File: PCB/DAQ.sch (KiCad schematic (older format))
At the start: 6 parts, among them J1 Arduino_Mega_Header, U1 SDshield, U2 RTC, U3 ADC, U4 NOKIA5110, U5 DAC

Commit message: PCB Improvement
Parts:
- added J2, J8: Conn_01x07, Pin_Headers:Pin_Header_Straight_1x07_Pitch2.54mm, symbol Conn_01x07
- added J3, J4, J7: Conn_01x08, Pin_Headers:Pin_Header_Straight_1x08_Pitch2.54mm, symbol Conn_01x08
- added J5: Conn_02x18_Counter_Clockwise, Pin_Headers:Pin_Header_Straight_2x18_Pitch2.54mm, symbol Conn_02x18_Counter_Clockwise
- added J6: Conn_01x10, Pin_Headers:Pin_Header_Straight_1x10_Pitch2.54mm, symbol Conn_01x10
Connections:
- net 3.3V: now also J2.3 (Pin_3)
- net 5V: now also J5.2 (Pin_2)
- net GND: now also J2.5 (Pin_5), J5.36 (Pin_36), J6.4 (Pin_4)
- net PIN2: now also J7.6 (Pin_6)
- net PIN3: now also J7.5 (Pin_5)
- net PIN31: now also J5.12 (Pin_12)
- net PIN33: now also J5.14 (Pin_14)
- net PIN35: now also J5.16 (Pin_16)
- net PIN4: now also J7.4 (Pin_4)
- net PIN5: now also J7.3 (Pin_3)
- net PIN50: now also J5.30 (Pin_30)
- net PIN51: now also J5.32 (Pin_32)
- net PIN52: now also J5.34 (Pin_34)
- net PIN6: now also J7.2 (Pin_2)
- net PIN7: now also J7.1 (Pin_1)
- net SCL: now also J6.1 (Pin_1)
- net SDA: now also J6.2 (Pin_2)
- new net 5v: J2.4 (Pin_4)
- no-connect marks 73 -> 137
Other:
- moved on the sheet: U1, U2, U3, U4, U5

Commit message: PCB Improvements
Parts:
- added C1: 100uF, Capacitors_THT:C_Axial_L12.0mm_D6.5mm_P15.00mm_Horizontal, symbol C
- added C2: 0.1uF, Capacitors_THT:CP_Axial_L11.0mm_D6.0mm_P18.00mm_Horizontal, symbol C
- added C3: 10uF, Capacitors_THT:CP_Axial_L11.0mm_D6.0mm_P18.00mm_Horizontal, symbol C
- added C4: 1uF, Capacitors_THT:CP_Axial_L11.0mm_D6.0mm_P18.00mm_Horizontal, symbol C
- added CC+1, CC-1: 0.01uF, Capacitors_THT:CP_Axial_L11.0mm_D6.0mm_P18.00mm_Horizontal, symbol C
- added CF+1, CF-1: 100uF, Capacitors_THT:C_Axial_L3.8mm_D2.6mm_P7.50mm_Horizontal, symbol C
- added DX+1, DX-1: D_Schottky, Diodes_THT:D_A-405_P12.70mm_Horizontal, symbol D_Schottky
- added IC1: MAX743CWE+, Housings_DIP:DIP-16_W7.62mm, symbol MAX743CWE+
- added LX+1, LX-1: 100uH, Inductors_THT:L_Axial_L9.5mm_D4.0mm_P12.70mm_Horizontal_Fastron_SMCC, symbol L
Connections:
- net 5V: now also C1.1, C2.2, IC1.12 (V+(3)), IC1.13 (V+(4)), IC1.3 (AV+), IC1.4 (V+(1)), IC1.5 (V+(2)), LX+1.1
- net GND: now also C1.2, CF+1.2, CF-1.2, IC1.11 (12/~15), IC1.14 (GND), LX-1.2
- net PIN2: now also U4.5 (CLK); no longer U4.1 (RST)
- net PIN3: now also U4.4 (DIN); no longer U4.2 (CE)
- net PIN6: now also U4.2 (CE); no longer U4.4 (DIN)
- net PIN7: now also U4.1 (RST); no longer U4.5 (CLK)
- new net: C2.1, C3.1, C4.1, CC+1.2, CC-1.2, IC1.2 (AGND)
- new net: C4.2, IC1.7 (SS)
- new net: C3.2, IC1.6 (VREF)
- new net: CC+1.1, IC1.1 (CC+)
- new net: DX+1.2 (A), IC1.15 (LX+), LX+1.2
- new net: DX-1.1 (K), IC1.10 (LX-), LX-1.1
- new net: CC-1.1, IC1.8 (CC-)
- new net +15V: CF+1.1, DX+1.1 (K), IC1.16 (FB+)
- new net -15V: CF-1.1, DX-1.2 (A), IC1.9 (FB-)

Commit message: Add ground plane,max743 and started analogic conditioner
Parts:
- added C5, C6, C7, C8: C, Resistors_THT:R_Axial_DIN0207_L6.3mm_D2.5mm_P7.62mm_Horizontal, symbol C
- added D1: LM4040, symbol LM4040
- added R1: 68k, Resistors_THT:R_Axial_DIN0207_L6.3mm_D2.5mm_P7.62mm_Horizontal, symbol R
- added R2: 18k, Resistors_THT:R_Axial_DIN0207_L6.3mm_D2.5mm_P7.62mm_Horizontal, symbol R
- added R3: 22k, Resistors_THT:R_Axial_DIN0207_L6.3mm_D2.5mm_P7.62mm_Horizontal, symbol R
- added R4, R8: 100k, Resistors_THT:R_Axial_DIN0207_L6.3mm_D2.5mm_P7.62mm_Horizontal, symbol R
- added R5: 200k, Resistors_THT:R_Axial_DIN0207_L6.3mm_D2.5mm_P7.62mm_Horizontal, symbol R
- added R6: 51k, Resistors_THT:R_Axial_DIN0207_L6.3mm_D2.5mm_P7.62mm_Horizontal, symbol R
- added R7: 47, Resistors_THT:R_Axial_DIN0207_L6.3mm_D2.5mm_P7.62mm_Horizontal, symbol R
- added U6, U7: LM358, Housings_DIP:DIP-8_W7.62mm, symbol LM358
- C1: footprint Capacitors_THT:C_Axial_L12.0mm_D6.5mm_P15.00mm_Horizontal -> Resistors_THT:R_Axial_DIN0204_L3.6mm_D1.6mm_P7.62mm_Horizontal
- C2, C3, C4, CC+1, CC-1: footprint Capacitors_THT:CP_Axial_L11.0mm_D6.0mm_P18.00mm_Horizontal -> Resistors_THT:R_Axial_DIN0204_L3.6mm_D1.6mm_P7.62mm_Horizontal
- CF+1, CF-1: footprint Capacitors_THT:C_Axial_L3.8mm_D2.6mm_P7.50mm_Horizontal -> Resistors_THT:R_Axial_DIN0204_L3.6mm_D1.6mm_P7.62mm_Horizontal
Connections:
- net -15V: now also U6.4 (V-), U6.4 (V-), U7.4 (V-)
- net GND: now also D1.2 (A), R2.2, R6.1, R7.2
- new net: R1.1, U6.1, U6.2 (-)
- new net: R8.1, U7.1
- new net: R7.1, R8.2, U7.2 (-)
- new net: R4.1, R5.1, R6.2, U7.3 (+)
- new net: R1.2, R2.1, U6.5 (+)
- new net: R4.2, U6.6 (-), U6.7
- new net: D1.1 (K), R3.2, R5.2
- new net 15V: R3.1, U6.8 (V+), U6.8 (V+), U7.8 (V+)
- no-connect marks 137 -> 142

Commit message: Analog Conditioner added int PCB layout
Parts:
- C5, C6, C7, C8: value C -> 100nF
- D1: footprint (none) -> TH-R:R-C-L-D
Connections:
- net -15V: now also C6.1, C7.2
- net 15V: now also C5.2, C8.2
- net GND: now also C5.1, C6.2, C7.1, C8.1
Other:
- moved on the sheet: C5, C6, C7, C8

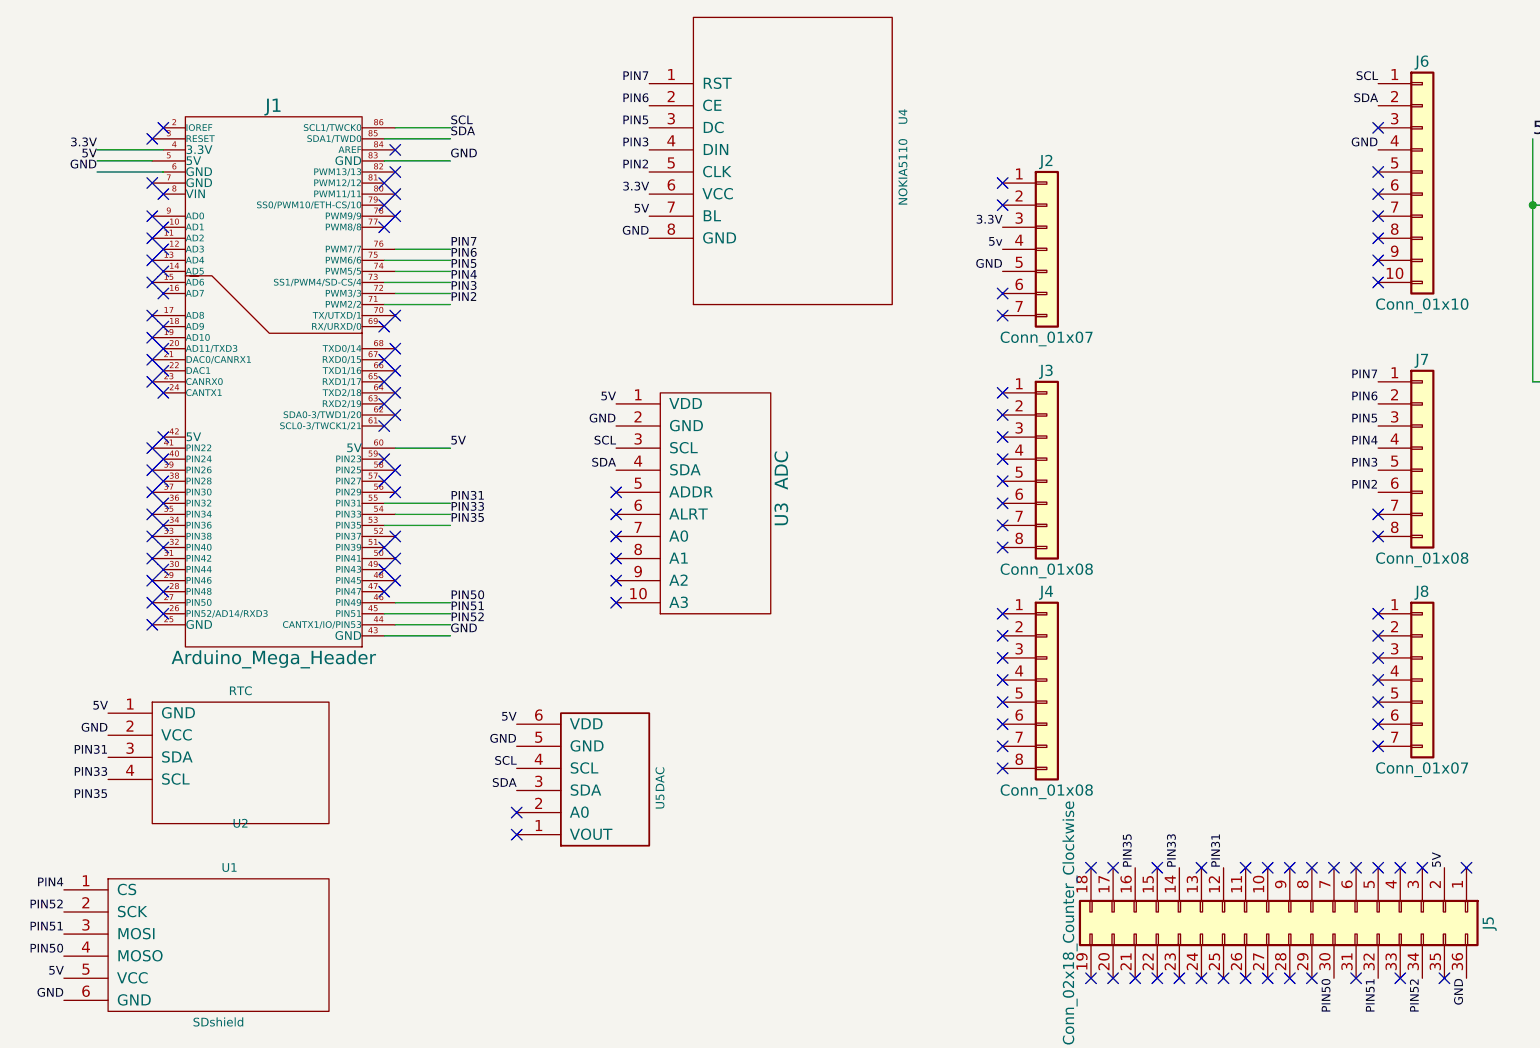
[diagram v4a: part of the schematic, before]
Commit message: Changed RTC module on PCB
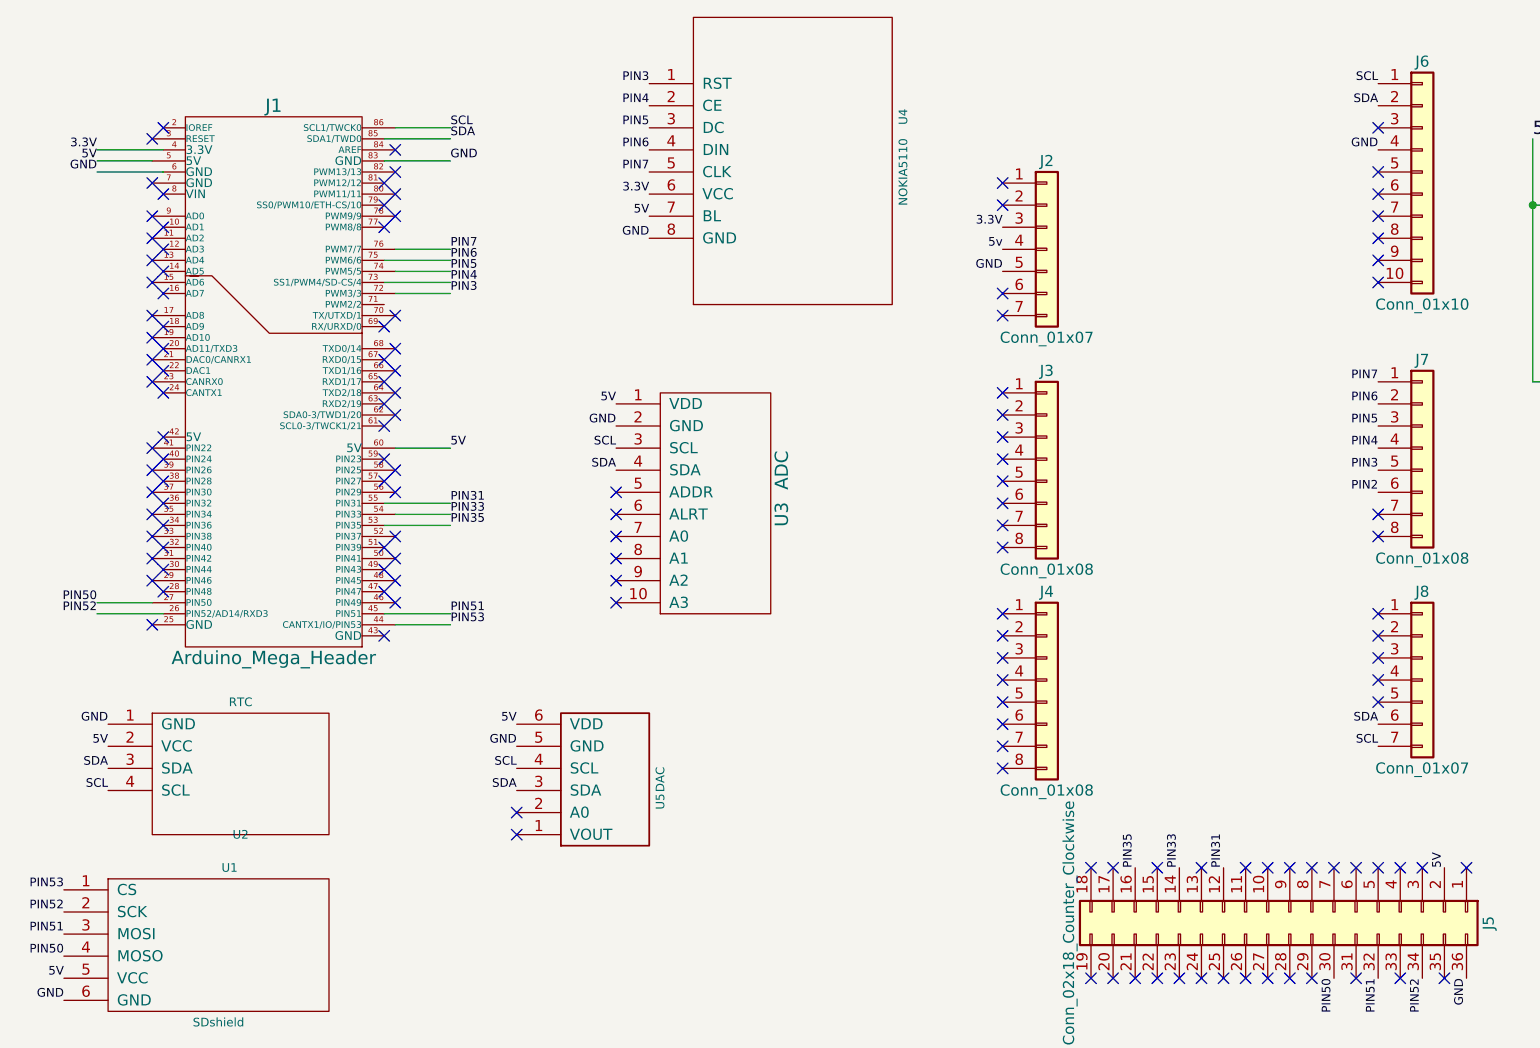
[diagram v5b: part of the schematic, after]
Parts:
- U2: footprint RTC:SDShield -> SDShield:SDShield
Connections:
- net 5V: now also U2.2 (VCC); no longer U2.1 (GND)
- net GND: now also U2.1 (GND); no longer J1.43 (GND), U2.2 (VCC)
- net PIN2: no longer J1.71 (PWM2/2), U4.5 (CLK)
- net PIN3: now also U4.1 (RST); no longer U4.4 (DIN)
- net PIN31: no longer U2.3 (SDA)
- net PIN33: no longer U2.4 (SCL)
- net PIN4: now also U4.2 (CE); no longer U1.1 (CS)
- net PIN50: now also J1.27 (PIN50); no longer J1.46 (PIN49)
- net PIN52: now also J1.26 (PIN52/AD14/RXD3); no longer J1.44 (CANTX1/IO/PIN53)
- net PIN6: now also U4.4 (DIN); no longer U4.2 (CE)
- net PIN7: now also U4.5 (CLK); no longer U4.1 (RST)
- net SCL: now also J8.7 (Pin_7), U2.4 (SCL)
- net SDA: now also J8.6 (Pin_6), U2.3 (SDA)
- new net PIN53: J1.44 (CANTX1/IO/PIN53), U1.1 (CS)
- no-connect marks 142 -> 140

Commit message: Improvements on the PCB
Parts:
- added J10, J11, J12, J9: Conn_01x01, Pin_Headers:Pin_Header_Straight_1x01_Pitch2.54mm, symbol Conn_01x01
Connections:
- net PIN50: now also J11.1 (Pin_1), J9.1 (Pin_1)
- net PIN52: now also J10.1 (Pin_1), J12.1 (Pin_1)
- net SCL: now also J1.61 (SCL0-3/TWCK1/21)
- net SDA: now also J1.62 (SDA0-3/TWD1/20)
- no-connect marks 140 -> 138
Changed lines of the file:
@@
 NoConn ~ 2450 3000
 NoConn ~ 2400 2950
-NoConn ~ 2400 2800
-NoConn ~ 2450 2750
 NoConn ~ 2400 2700
 NoConn ~ 2450 2650
@@
 Text Label 1150 4450 2    39   ~ 0
 SCL
+Wire Wire Line
+	2450 2750 2700 2750
+Wire Wire Line
+	2400 2800 2700 2800
+Text Label 2700 2750 0    39   ~ 0
+SDA
+Text Label 2700 2800 0    39   ~ 0
+SCL
+Text Label 6900 4250 2    39   ~ 0
+SCL
 Text Label 6900 4150 2    39   ~ 0
 SDA
-Text Label 6900 4250 2    39   ~ 0
-SCL
+$Comp
+L Conn_01x01 J11
+U 1 1 5AC6A77C
+P 4450 4600
+F 0 "J11" H 4450 4700 50  0000 C CNN
+F 1 "Conn_01x01" H 4450 4500 50  0000 C CNN
+F 2 "Pin_Headers:Pin_Header_Straight_1x01_Pitch2.54mm" H 4450 4600 50  0001 C CNN
+F 3 "" H 4450 4600 50  0001 C CNN
+	1    4450 4600
+	1    0    0    -1
+$EndComp
+$Comp
+L Conn_01x01 J12
+U 1 1 5AC6A7F5
+P 4450 4900
+F 0 "J12" H 4450 5000 50  0000 C CNN
+F 1 "Conn_01x01" H 4450 4800 50  0000 C CNN
+F 2 "Pin_Headers:Pin_Header_Straight_1x01_Pitch2.54mm" H 4450 4900 50  0001 C CNN
+F 3 "" H 4450 4900 50  0001 C CNN
+	1    4450 4900
+	1    0    0    -1
+$EndComp
+$Comp
+L Conn_01x01 J9
+U 1 1 5AC6A961
+P 3800 4900
+F 0 "J9" H 3800 5000 50  0000 C CNN
+F 1 "Conn_01x01" H 3800 4800 50  0000 C CNN
+F 2 "Pin_Headers:Pin_Header_Straight_1x01_Pitch2.54mm" H 3800 4900 50  0001 C CNN
+F 3 "" H 3800 4900 50  0001 C CNN
+	1    3800 4900
+	1    0    0    -1
+$EndComp
+$Comp
+L Conn_01x01 J10
+U 1 1 5AC6A967
+P 3800 5200
+F 0 "J10" H 3800 5300 50  0000 C CNN
+F 1 "Conn_01x01" H 3800 5100 50  0000 C CNN
+F 2 "Pin_Headers:Pin_Header_Straight_1x01_Pitch2.54mm" H 3800 5200 50  0001 C CNN
+F 3 "" H 3800 5200 50  0001 C CNN
+	1    3800 5200
+	1    0    0    -1
+$EndComp
+Text Label 3600 4900 2    39   ~ 0
+PIN50
+Text Label 4250 4600 2    39   ~ 0
+PIN50
+Text Label 4250 4900 2    39   ~ 0
+PIN52
+Text Label 3600 5200 2    39   ~ 0
+PIN52
 $EndSCHEMATC
